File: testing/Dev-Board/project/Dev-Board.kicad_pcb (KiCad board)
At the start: 2 copper layers, 76 parts, among them IC101 BQ51013B, IC102 MAX32664, IC103 MAX30101, IC104 NPM1100-QDAA-R, IC105 TPS61240, IC106 KXTJ3-1057, Q101 BSS138, Q102 BSH205G2AR, X101 BATTERY, X102 INTERFACE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

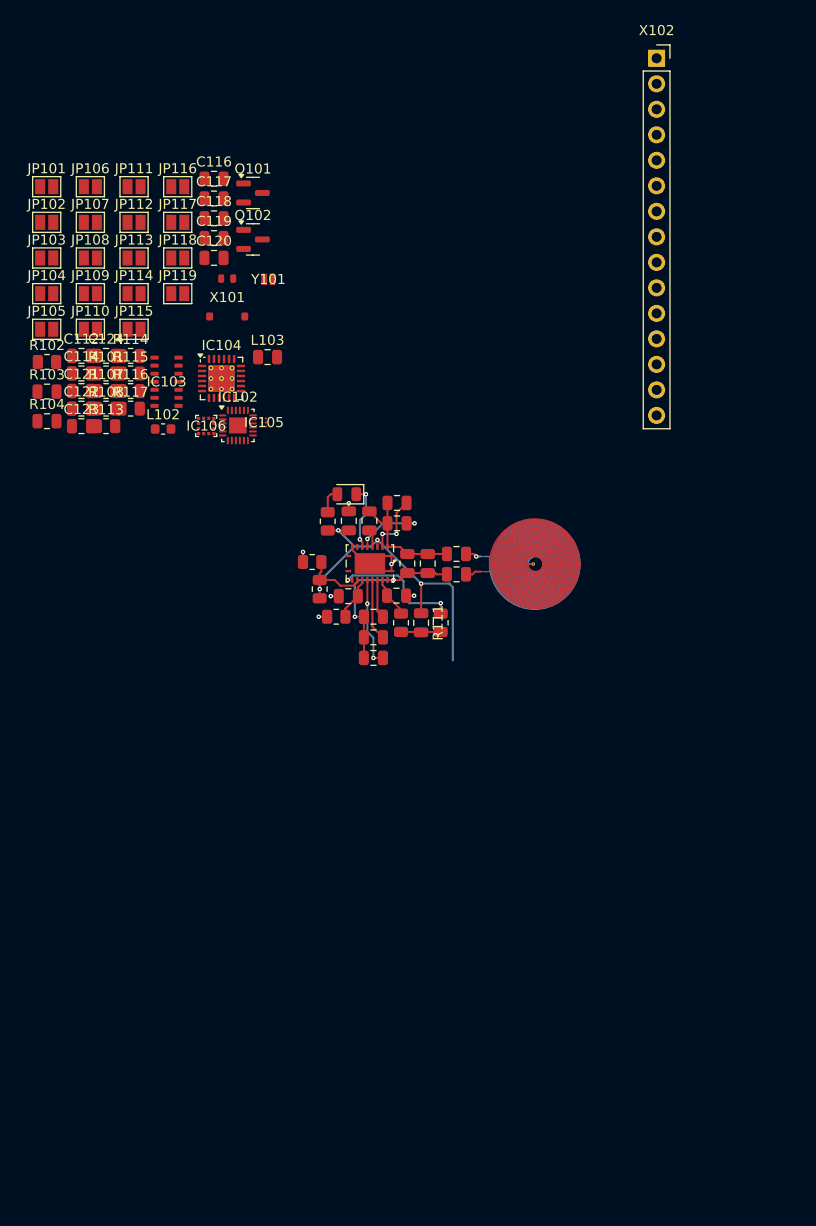
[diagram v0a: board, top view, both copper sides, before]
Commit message: Add layout for Dev-Board
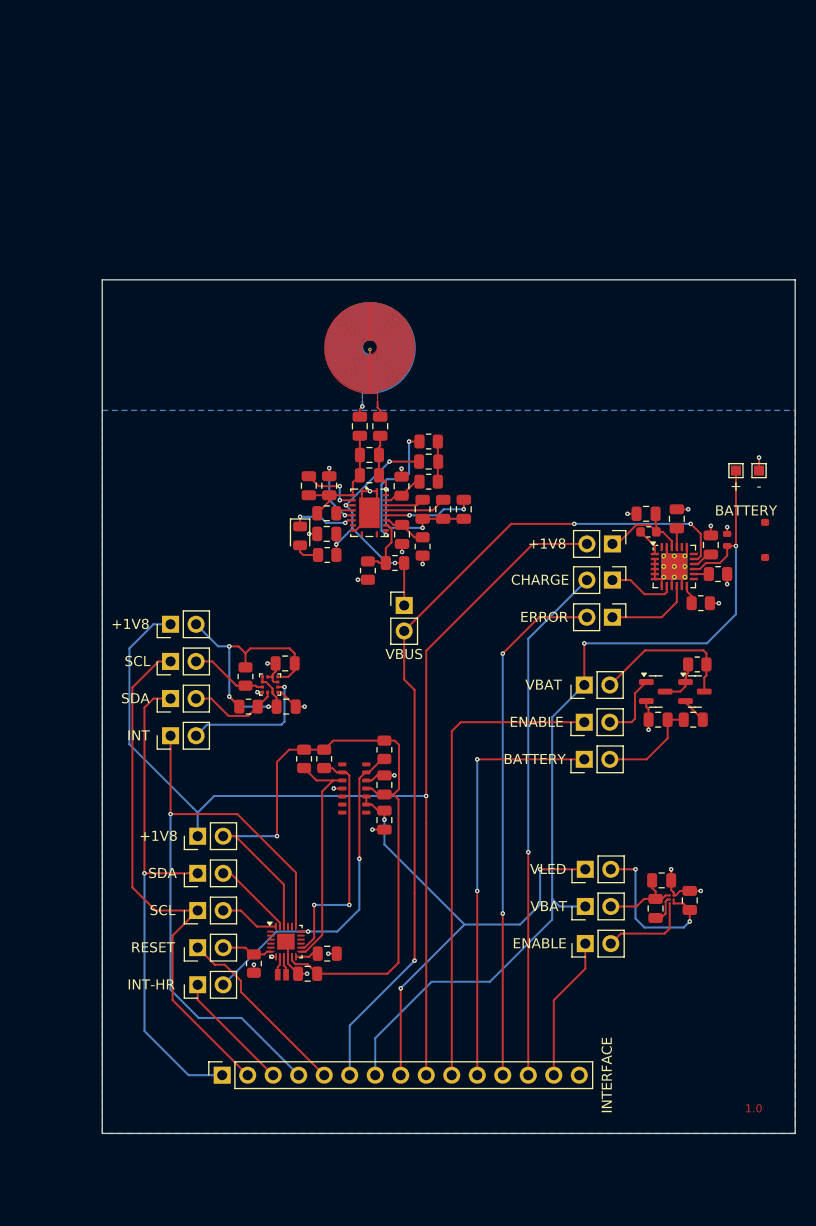
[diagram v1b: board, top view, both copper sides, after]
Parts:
- removed the R114 at (91.8, 70.6)
- added TH102: Thermistor_NTC, Resistor_SMD:R_0805_2012Metric, F.Cu at (150.3, 92.3)
- added TP101: +, TestPoint:TestPoint_Pad_1.0x1.0mm, F.Cu at (152.1, 82.0)
- added TP102: -, TestPoint:TestPoint_Pad_1.0x1.0mm, F.Cu at (154.4, 82.0)
- JP101, JP102, JP103, JP104, JP105, JP106, JP107, JP108, JP109, JP110, JP111, JP112, JP113, JP114, JP115, JP116, JP117, JP118, JP119: footprint Jumper:SolderJumper-2_P1.3mm_Open_Pad1.0x1.5mm -> Connector_PinHeader_2.54mm:PinHeader_1x02_P2.54mm_Vertical
- moved X102 110.1 mm to (100.9, 142.2), turned to 90 degrees
- moved C124 79.5 mm to (147.5, 124.8), turned to 90 degrees
- moved JP115 75.9 mm to (137.1, 129.1), turned to 90 degrees
- moved JP114 75.8 mm to (137.1, 125.4), turned to 90 degrees
- moved JP113 75.7 mm to (137.1, 121.7), turned to 90 degrees
- moved C121 75.6 mm to (144.7, 122.8)
- moved JP103 73.2 mm to (137.0, 110.8), turned to 90 degrees
- moved JP108 73.2 mm to (98.5, 133.2), turned to 90 degrees
- moved JP102 73.1 mm to (137.0, 107.0), turned to 90 degrees
- moved JP101 73.0 mm to (137.0, 103.3), turned to 90 degrees
- moved JP106 72.9 mm to (98.5, 125.8), turned to 90 degrees
- moved R103 72.2 mm to (147.8, 106.8), turned to 180 degrees
- moved R102 71.4 mm to (148.2, 101.3), turned to 180 degrees
- moved Y101 69.3 mm to (106.9, 132.2)
- moved R104 67.7 mm to (144.3, 106.8), turned to 180 degrees
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- renumbered R115 to R114, R116 to R115, R117 to R116
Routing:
- net +1V8: track 0.00 -> 112.7 mm, vias 0 -> 1
- net V_{DD}: track 0.00 -> 107.0 mm, vias 0 -> 4
- net /V_{BAT}: track 0.00 -> 95.0 mm, vias 0 -> 2
- net /V_{BUS}: track 0.00 -> 84.7 mm, vias 0 -> 3
- net /Int-Acc: track 0.00 -> 61.8 mm, vias 0 -> 1
- net /SCL: track 0.00 -> 52.8 mm
- net /Error: track 0.00 -> 51.9 mm, vias 0 -> 2
- net /Charge: track 0.00 -> 51.7 mm, vias 0 -> 1
- net V_{LED}: track 0.00 -> 51.5 mm, vias 0 -> 3
- net /SDA: track 0.00 -> 50.0 mm, vias 0 -> 1
- net /Battery-Enable: track 0.00 -> 47.8 mm
- net GND: track 13.3 -> 55.5 mm, vias 6 -> 26
- net /Battery: track 0.00 -> 42.1 mm, vias 0 -> 2
- net Net-(IC102-Int-HR): track 0.00 -> 33.7 mm, vias 0 -> 2
- net Net-(IC102-SCL-Sensor): track 0.00 -> 24.2 mm, vias 0 -> 2
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- added copper zone on B.Cu, net GND
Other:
- board outline added: 69 x 85 mm
- board text added: "1.0"

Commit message: Changes from Jakob
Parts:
- removed JP111: CHARGE, Connector_PinHeader_2.54mm:PinHeader_1x02_P2.54mm_Vertical
- removed JP112: ERROR, Connector_PinHeader_2.54mm:PinHeader_1x02_P2.54mm_Vertical
- C121: value 4u7 -> 2u2
- R107: value 1k -> 18k
- R108: value 1k -> 1k8
- X102: footprint Connector_PinSocket_2.54mm:PinSocket_1x15_P2.54mm_Vertical -> Connector_PinHeader_2.54mm:PinHeader_1x21_P2.54mm_Vertical
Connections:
- C118 pad 1: Net-(IC104-VSYS) -> /V_{SYS}
- IC101 pad 10: unconnected-(IC101-EN1-Pad10) -> /EN1
- IC101 pad 11: unconnected-(IC101-EN2-Pad11) -> /EN2
- IC102 pad 13: Net-(IC102-SDA-Sensor) -> /SDA-Slave
- IC102 pad 14: Net-(IC102-SCL-Sensor) -> /SCL-Slave
- IC103 pad 2: Net-(IC102-SCL-Sensor) -> /SCL-Slave
- IC103 pad 3: Net-(IC102-SDA-Sensor) -> /SDA-Slave
- IC104 pad 10: Net-(IC104-ERR) -> /Error
- IC104 pad 11: GND -> /SHPHLD
- IC104 pad 16: Net-(IC104-VSYS) -> /V_{SYS}
- IC104 pad 6: GND -> /SHPACT
- IC104 pad 8: Net-(IC104-CHG) -> /Charge
- JP114 pad 1: /V_{BAT} -> /V_{SYS}
- R107 pad 2: Net-(IC102-SDA-Sensor) -> /SDA-Slave
- R108 pad 2: Net-(IC102-SCL-Sensor) -> /SCL-Slave
- X102 pad 15: GND -> /SDA-Slave
- X102 pad 7: /V_{BAT} -> /V_{SYS}
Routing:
- net /V_{SYS}: track 0.00 -> 83.8 mm, vias 0 -> 3
- net /EN1: track 0.00 -> 83.2 mm, vias 0 -> 1
- net /EN2: track 0.00 -> 82.6 mm, vias 0 -> 1
- net /SCL-Slave: track 0.00 -> 62.0 mm, vias 0 -> 4
- net /SDA-Slave: track 0.00 -> 60.9 mm, vias 0 -> 3
- net /SHPACT: track 0.00 -> 57.0 mm, vias 0 -> 2
- net /V_{BAT}: track 95.0 -> 39.9 mm, vias 2 -> 1
- net /SHPHLD: track 0.00 -> 52.5 mm
- net Net-(IC102-SCL-Sensor): track 24.2 -> 0.00 mm, vias 2 -> 0
- net Net-(IC102-SDA-Sensor): track 23.0 -> 0.00 mm
- net /Error: track 51.9 -> 63.0 mm
- net Net-(IC104-ERR): track 8.64 -> 0.00 mm
- net /Charge: track 51.7 -> 59.8 mm, vias 1 -> 2
- net Net-(IC104-CHG): track 6.03 -> 0.00 mm
- net GND: track 55.5 -> 52.2 mm
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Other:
- board size 69 x 85 mm -> 69 x 91 mm
- board text added: "1V8"
- board text added: "Battery"
- board text added: "Battery-Enable"
- board text added: "Charge"
- board text added: "EN1"
- board text added: "EN2"
- board text added: "Error"
- board text added: "GND"
- board text added: "Int-Acc"
- board text added: "Int-HR"
- board text added: "LED-Enable"
- board text added: "SCL"
- board text added: "SCL-Slave"
- board text added: "SDA"
- board text added: "SDA-Slave"
- board text added: "SHPACT"
- board text added: "V_{BUS}"
- board text added: "V_{LED}"
- board text added: "V_{SYS}"
- board text added: "~{HR-Reset}"

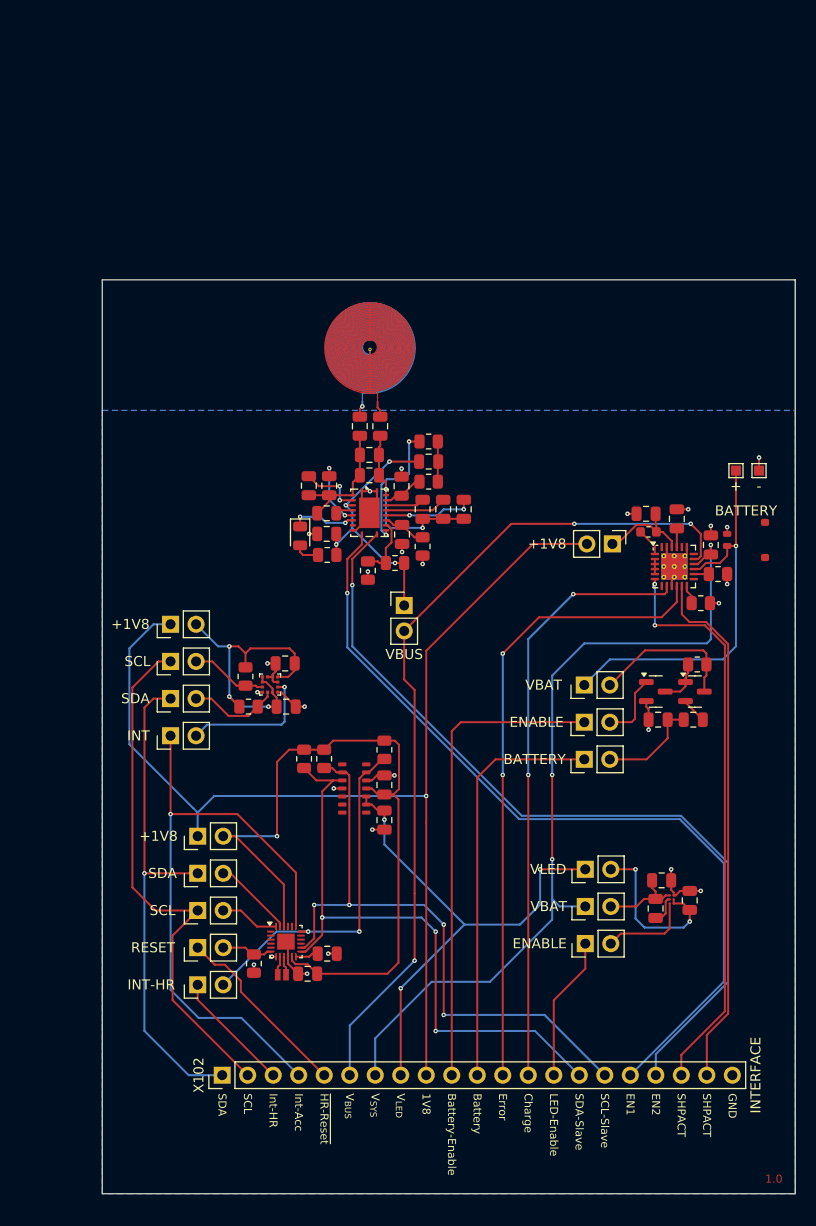
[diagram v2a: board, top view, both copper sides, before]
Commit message: Cosmetic changes only. Silkscreen and edge cuts.
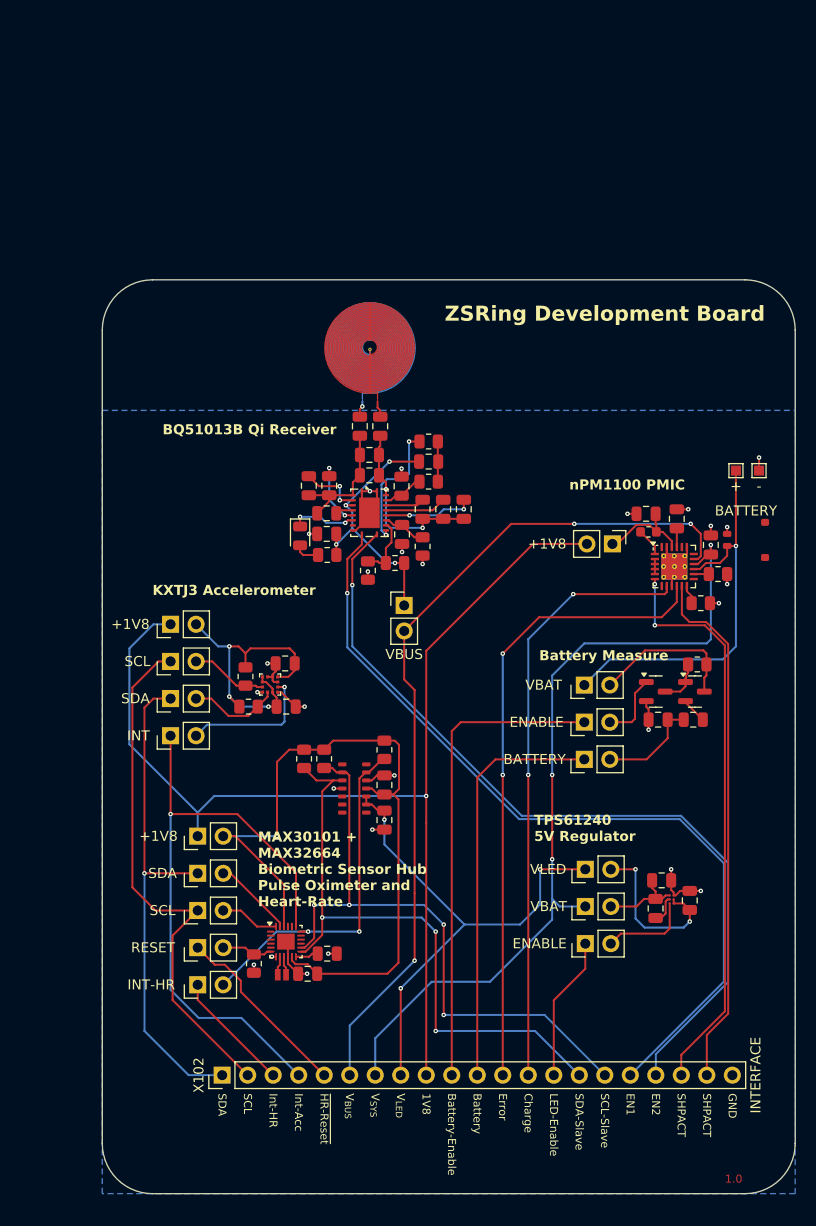
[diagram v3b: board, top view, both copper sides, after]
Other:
- outline, holes or cut-outs redrawn
- board text added: "BQ51013B Qi Receiver"
- board text added: "Battery Measure"
- board text added: "KXTJ3 Accelerometer"
- board text added: "MAX30101 + MAX32664 Biometric Sensor Hub Pulse Oximeter and Heart-Rate"
- board text added: "TPS61240 5V Regulator"
- board text added: "ZSRing Development Board"
- board text added: "nPM1100 PMIC"
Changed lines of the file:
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@@
 		)
 	)
-	(gr_rect
-		(start 89 63)
-		(end 158 154)
-		(stroke
-			(width 0.1)
-			(type default)
-		)
-		(fill none)
+	(gr_arc
+		(start 89 68)
+		(mid 90.464466 64.464466)
+		(end 94 63)
+		(stroke
+			(width 0.05)
+			(type default)
+		)
+		(layer "Edge.Cuts")
+	)
+	(gr_arc
+		(start 158 149)
+		(mid 156.535534 152.535534)
+		(end 153 154)
+		(stroke
+			(width 0.05)
+			(type default)
+		)
+		(layer "Edge.Cuts")
+	)
+	(gr_line
+		(start 158 68)
+		(end 158 149)
+		(stroke
+			(width 0.05)
+			(type default)
+		)
+		(layer "Edge.Cuts")
+	)
+	(gr_line
+		(start 89 149)
+		(end 89 68)
+		(stroke
+			(width 0.05)
+			(type default)
+		)
+		(layer "Edge.Cuts")
+	)
+	(gr_line
+		(start 153 154)
+		(end 94 154)
+		(stroke
+			(width 0.05)
+			(type default)
+		)
+		(layer "Edge.Cuts")
+	)
+	(gr_arc
+		(start 94 154)
+		(mid 90.464466 152.535534)
+		(end 89 149)
+		(stroke
+			(width 0.05)
+			(type default)
+		)
+		(layer "Edge.Cuts")
+	)
+	(gr_arc
+		(start 153 63)
+		(mid 156.535534 64.464466)
+		(end 158 68)
+		(stroke
+			(width 0.05)
+			(type default)
+		)
+		(layer "Edge.Cuts")
+	)
+	(gr_line
+		(start 94 63)
+		(end 153 63)
+		(stroke
+			(width 0.05)
+			(type default)
+		)
 		(layer "Edge.Cuts")
 	)
 	(gr_text "1.0"
-		(at 155 153 0)
+		(at 151 153 0)
 		(layer "F.Cu")
 		(effects
@@
 		)
 	)
+	(gr_text "Battery Measure"
+		(at 132.5 101 0)
+		(layer "F.SilkS")
+		(effects
+			(font
+				(size 1 1)
+				(thickness 0.16)
+				(bold yes)
+			)
+			(justify left bottom)
+		)
+	)
+	(gr_text "ZSRing Development Board"
+		(at 155 65.5 0)
+		(layer "F.SilkS")
+		(effects
+			(font
+				(size 1.5 1.5)
+				(thickness 0.3)
+				(bold yes)
+			)
+			(justify right top)
+		)
+	)
 	(gr_text "SHPACT"
 		(at 149.2 144 270)
@@
 		)
 	)
+	(gr_text "BQ51013B Qi Receiver"
+		(at 95 78.5 0)
+		(layer "F.SilkS")
+		(effects
+			(font
+				(size 1 1)
+				(thickness 0.16)
+				(bold yes)
+			)
+			(justify left bottom)
+		)
+	)
+	(gr_text "MAX30101 +\nMAX32664\nBiometric Sensor Hub\nPulse Oximeter and\nHeart-Rate "
+		(at 104.5 125.5 0)
+		(layer "F.SilkS")
+		(effects
+			(font
+				(size 1 1)
+				(thickness 0.16)
+				(bold yes)
+			)
+			(justify left bottom)
+		)
+	)
 	(gr_text "~{HR-Reset}"
 		(at 111.1 144 270)
@@
 		)
 	)
+	(gr_text "KXTJ3 Accelerometer"
+		(at 94 94.5 0)
+		(layer "F.SilkS")
+		(effects
+			(font
+				(size 1 1)
+				(thickness 0.16)
+				(bold yes)
+			)
+			(justify left bottom)
+		)
+	)
+	(gr_text "nPM1100 PMIC"
+		(at 135.5 84 0)
+		(layer "F.SilkS")
+		(effects
+			(font
+				(size 1 1)
+				(thickness 0.16)
+				(bold yes)
+			)
+			(justify left bottom)
+		)
+	)
 	(gr_text "V_{LED}"
 		(at 118.72 144 270)
@@
 		)
 	)
+	(gr_text "TPS61240\n5V Regulator"
+		(at 132 119 0)
+		(layer "F.SilkS")
+		(effects
+			(font
+				(size 1 1)
+				(thickness 0.16)
+				(bold yes)
+			)
+			(justify left bottom)
+		)
+	)
